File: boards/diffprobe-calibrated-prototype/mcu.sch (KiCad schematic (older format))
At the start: 2 parts

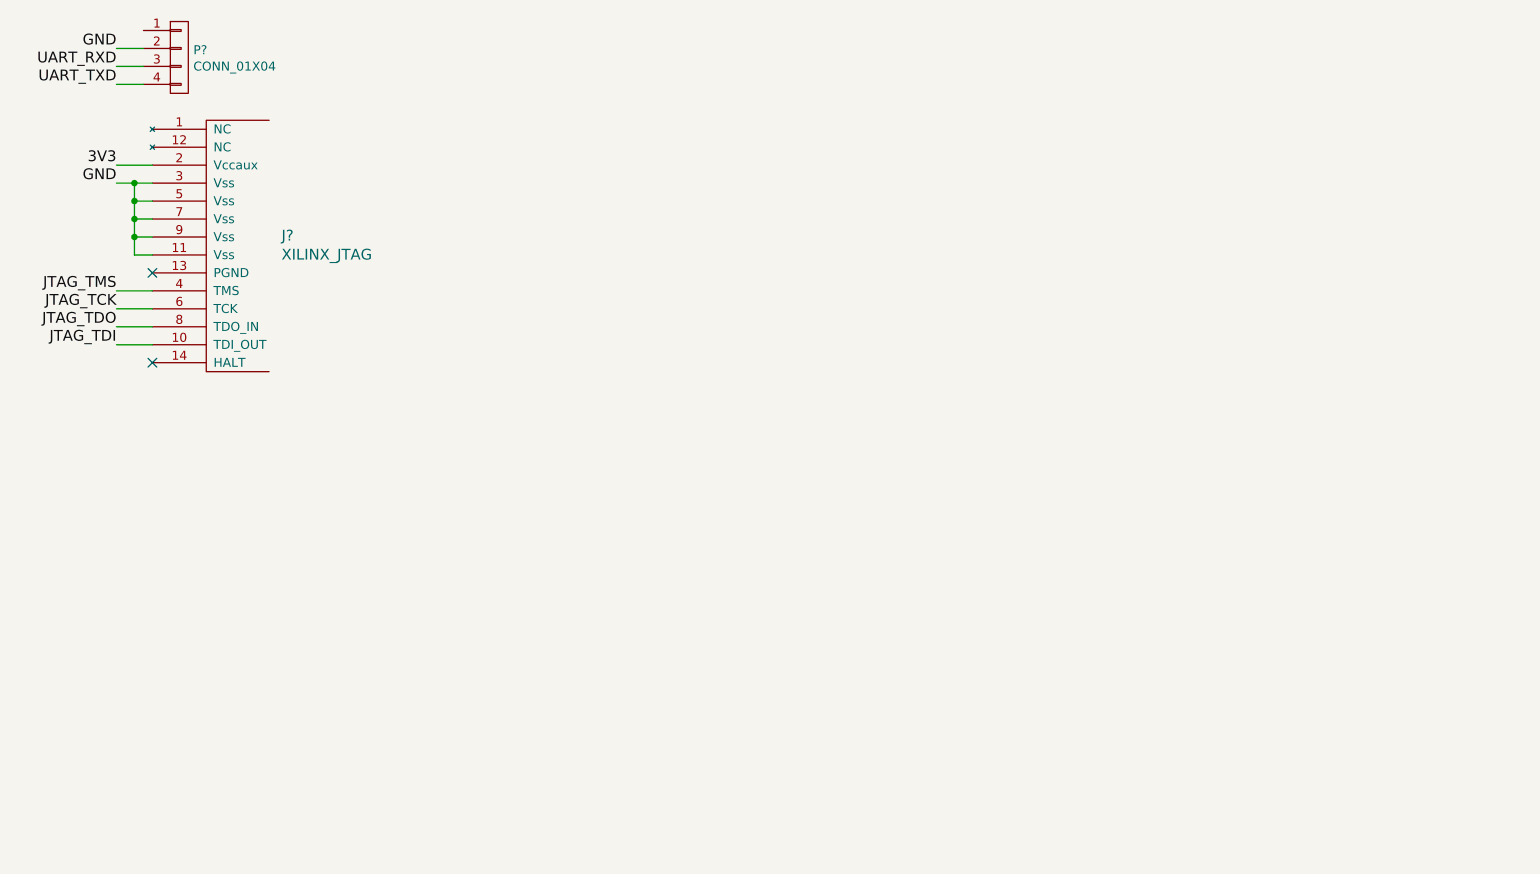
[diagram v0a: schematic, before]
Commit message: Continued work on differential probe
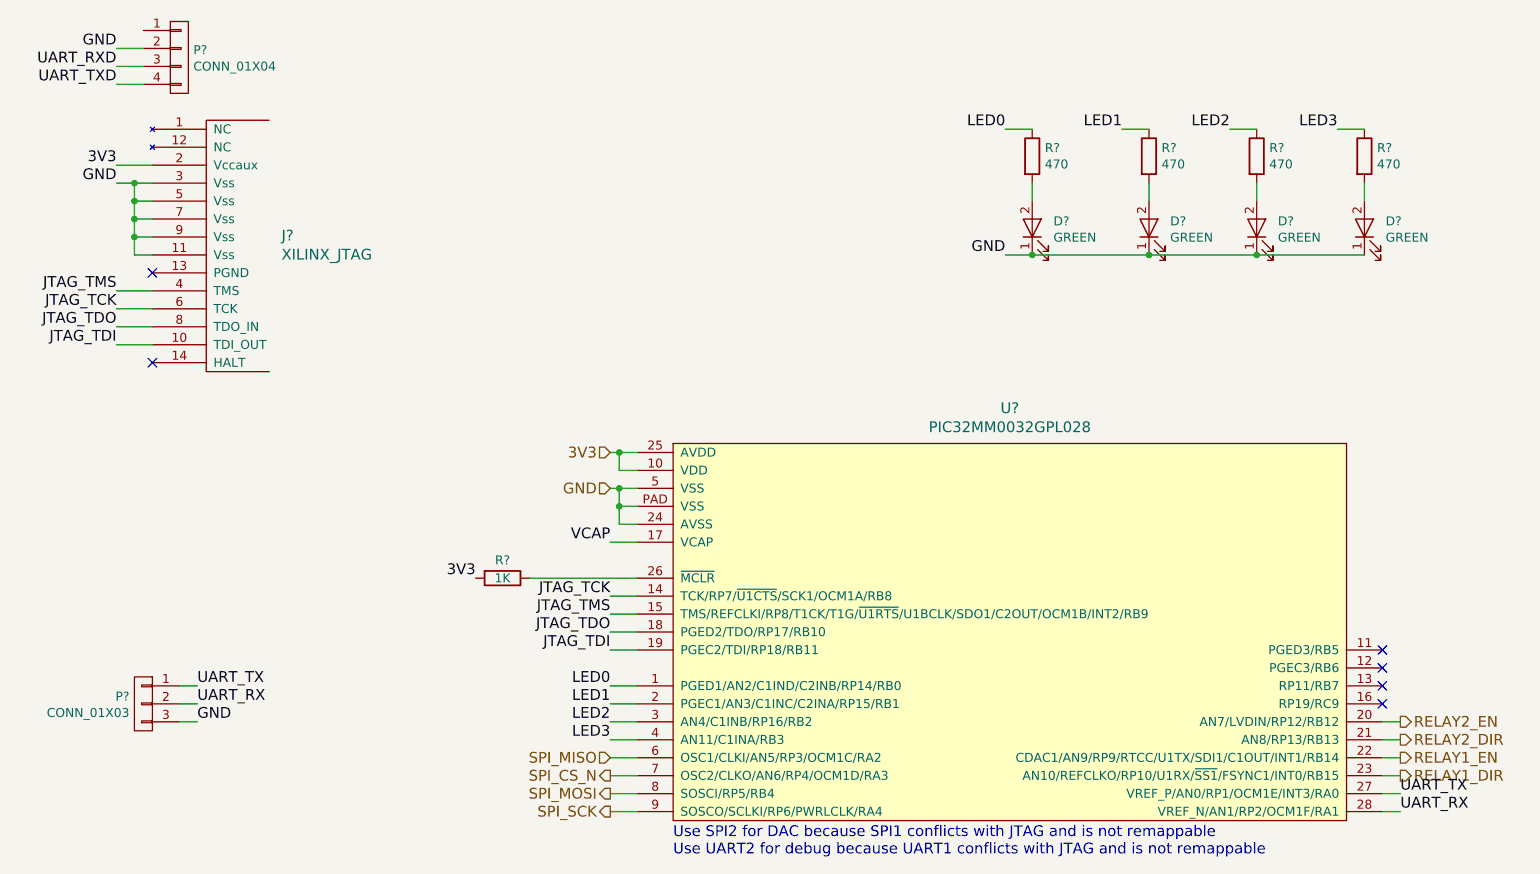
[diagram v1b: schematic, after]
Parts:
- added D? (x4): GREEN, symbol LED
- added P?: CONN_01X03, symbol CONN_01X03
- added R?: 1K, symbol R
- added R? (x4): 470, symbol R
- added U?: PIC32MM0032GPL028, symbol PIC32MMxGPL028
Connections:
- net 3V3: now also R?.2, U?.10 (VDD), U?.25 (AVDD)
- net GND: now also D?.1 (K), D?.1 (K), D?.1 (K), D?.1 (K), P?.3 (P3), U?.24 (AVSS), U?.5 (VSS), U?.PAD (VSS)
- net JTAG_TCK: now also U?.14 (TCK/RP7/~U1CTS~/SCK1/OCM1A/RB8)
- net JTAG_TDI: now also U?.19 (PGEC2/TDI/RP18/RB11)
- net JTAG_TDO: now also U?.18 (PGED2/TDO/RP17/RB10)
- net JTAG_TMS: now also U?.15 (TMS/REFCLKI/RP8/T1CK/T1G/~U1RTS~/U1BCLK/SDO1/C2OUT/OCM1B/INT2/RB9)
- new net: R?.1, U?.26 (~MCLR)
- new net: D?.2 (A), R?.2 (x4)
- new net LED0: R?.1, U?.1 (PGED1/AN2/C1IND/C2INB/RP14/RB0)
- new net LED1: R?.1, U?.2 (PGEC1/AN3/C1INC/C2INA/RP15/RB1)
- new net LED2: R?.1, U?.3 (AN4/C1INB/RP16/RB2)
- new net LED3: R?.1, U?.4 (AN11/C1INA/RB3)
- new net RELAY1_DIR: U?.23 (AN10/REFCLKO/RP10/U1RX/~SS1~/FSYNC1/INT0/RB15)
- new net RELAY1_EN: U?.22 (CDAC1/AN9/RP9/RTCC/U1TX/SDI1/C1OUT/INT1/RB14)
- new net RELAY2_DIR: U?.21 (AN8/RP13/RB13)
- new net RELAY2_EN: U?.20 (AN7/LVDIN/RP12/RB12)
- new net SPI_CS_N: U?.7 (OSC2/CLKO/AN6/RP4/OCM1D/RA3)
- new net SPI_MISO: U?.6 (OSC1/CLKI/AN5/RP3/OCM1C/RA2)
- new net SPI_MOSI: U?.8 (SOSCI/RP5/RB4)
- new net SPI_SCK: U?.9 (SOSCO/SCLKI/RP6/PWRLCLK/RA4)
- new net UART_RX: P?.2 (P2), U?.28 (VREF_N/AN1/RP2/OCM1F/RA1)
- new net UART_TX: P?.1 (P1), U?.27 (VREF_P/AN0/RP1/OCM1E/INT3/RA0)
- new net VCAP: U?.17 (VCAP)
- no-connect marks 2 -> 6
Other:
- note added: "Use SPI2 for DAC because SPI1 conflicts with JTAG and is not remappable\nUse UART2 for debug because UART1 conflicts with JTAG and is not remappable"

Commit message: Finished adding decoupling caps etc. Still needs signoff review.
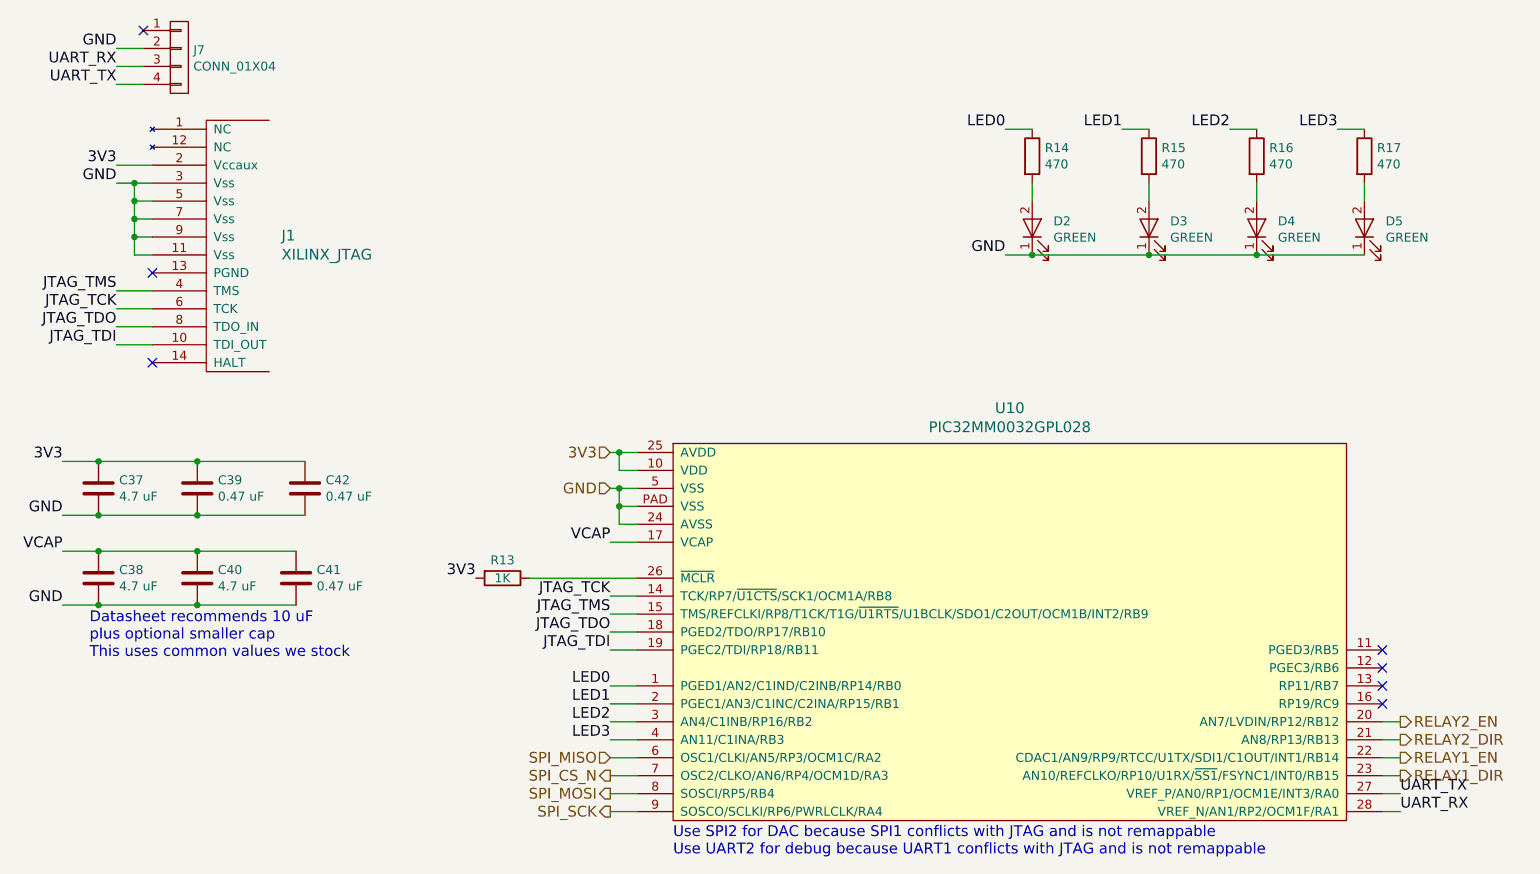
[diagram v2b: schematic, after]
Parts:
- removed P?: CONN_01X03, symbol CONN_01X03
- added C37, C38, C40: 4.7 uF, symbol C
- added C39, C41, C42: 0.47 uF, symbol C
- gave numbers to parts that had none: 12
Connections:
- net UART_RXD is gone; now on net UART_RX: J7.3 (P3)
- net UART_TXD is gone; now on net UART_TX: J7.4 (P4)
- net 3V3: now also C37.1, C39.1, C42.1
- net GND: now also C37.2, C38.2, C39.2, C40.2, C41.2, C42.2
- net VCAP: now also C38.1, C40.1, C41.1
- no-connect marks 6 -> 7
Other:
- note added: "Datasheet recommends 10 uF\nplus optional smaller cap\nThis uses common values we stock"
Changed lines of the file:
@@
 Sheet 4 4
 Title "500 MHz Active Differential Probe"
-Date "2017-12-18"
+Date "2017-12-19"
 Rev "0.2"
 Comp "Andrew D. Zonenberg"
@@
 $EndDescr
 $Comp
-L CONN_01X04 P?
+L CONN_01X04 J7
 U 1 1 5A1F8A2F
 P 1400 1100
-F 0 "P?" H 1478 1141 50  0000 L CNN
+F 0 "J7" H 1478 1141 50  0000 L CNN
 F 1 "CONN_01X04" H 1478 1050 50  0000 L CNN
 F 2 "" H 1400 1100 50  0000 C CNN
@@
 $EndComp
 Text Label 1050 1150 2    60   ~ 0
-UART_RXD
+UART_RX
 Wire Wire Line
 	1050 1050 1200 1050
@@
 	1050 1150 1200 1150
 Text Label 1050 1250 2    60   ~ 0
-UART_TXD
+UART_TX
 Wire Wire Line
 	1050 1250 1200 1250
 $Comp
-L XILINX_JTAG J?
+L XILINX_JTAG J1
 U 1 1 5A1F8B4D
 P 1250 2800
-F 0 "J?" H 1969 3508 60  0000 L CNN
+F 0 "J1" H 1969 3508 60  0000 L CNN
 F 1 "XILINX_JTAG" H 1969 3402 60  0000 L CNN
 F 2 "" H 1250 2800 60  0000 C CNN
@@
 NoConn ~ 1250 2800
 $Comp
-L PIC32MMxGPL028 U?
+L PIC32MMxGPL028 U10
 U 1 1 5A2E3505
 P 4150 5350
-F 0 "U?" H 6025 7647 60  0000 C CNN
+F 0 "U10" H 6025 7647 60  0000 C CNN
 F 1 "PIC32MM0032GPL028" H 6025 7541 60  0000 C CNN
 F 2 "" H 4150 5350 60  0001 C CNN
@@
 Wire Wire Line
 	3950 5300 3800 5300
-$Comp
-L CONN_01X03 P?
-U 1 1 5A363949
-P 1200 4700
-F 0 "P?" H 1278 4741 50  0000 L CNN
-F 1 "CONN_01X03" H 1278 4650 50  0000 L CNN
-F 2 "" H 1200 4700 50  0000 C CNN
-F 3 "" H 1200 4700 50  0000 C CNN
-	1    1200 4700
-	-1   0    0    -1
-$EndComp
-Text Label 1500 4600 0    60   ~ 0
-UART_TX
-Text Label 1500 4700 0    60   ~ 0
-UART_RX
-Text Label 1500 4800 0    60   ~ 0
-GND
 Text Label 1050 1050 2    60   ~ 0
 GND
-Wire Wire Line
-	1500 4600 1400 4600
-Wire Wire Line
-	1400 4700 1500 4700
-Wire Wire Line
-	1500 4800 1400 4800
 Text Label 8200 5200 0    60   ~ 0
 UART_TX
@@
 	8100 4900 8200 4900
 $Comp
-L R R?
+L R R13
 U 1 1 5A386F8B
 P 3200 4000
-F 0 "R?" V 3100 4000 50  0000 C CNN
+F 0 "R13" V 3100 4000 50  0000 C CNN
 F 1 "1K" V 3200 4000 50  0000 C CNN
 F 2 "" V 3130 4000 50  0000 C CNN
@@
 3V3
 $Comp
-L R R?
+L R R14
 U 1 1 5A3872CE
 P 6150 1650
-F 0 "R?" H 6220 1696 50  0000 L CNN
+F 0 "R14" H 6220 1696 50  0000 L CNN
 F 1 "470" H 6220 1605 50  0000 L CNN
 F 2 "" V 6080 1650 50  0000 C CNN
@@
 $EndComp
 $Comp
-L LED D?
+L LED D2
 U 1 1 5A387391
 P 6150 2050
-F 0 "D?" V 6188 1932 50  0000 R CNN
+F 0 "D2" V 6188 1932 50  0000 R CNN
 F 1 "GREEN" V 6097 1932 50  0000 R CNN
 F 2 "" H 6150 2050 50  0000 C CNN
@@
 	6000 2200 8000 2200
 $Comp
-L R R?
+L R R15
 U 1 1 5A3875D8
 P 6800 1650
-F 0 "R?" H 6870 1696 50  0000 L CNN
+F 0 "R15" H 6870 1696 50  0000 L CNN
 F 1 "470" H 6870 1605 50  0000 L CNN
 F 2 "" V 6730 1650 50  0000 C CNN
@@
 $EndComp
 $Comp
-L LED D?
+L LED D3
 U 1 1 5A3875DE
 P 6800 2050
-F 0 "D?" V 6838 1932 50  0000 R CNN
+F 0 "D3" V 6838 1932 50  0000 R CNN
 F 1 "GREEN" V 6747 1932 50  0000 R CNN
 F 2 "" H 6800 2050 50  0000 C CNN
@@
 	6650 1500 6800 1500
 $Comp
-L R R?
+L R R16
 U 1 1 5A387669
 P 7400 1650
-F 0 "R?" H 7470 1696 50  0000 L CNN
+F 0 "R16" H 7470 1696 50  0000 L CNN
 F 1 "470" H 7470 1605 50  0000 L CNN
 F 2 "" V 7330 1650 50  0000 C CNN
@@
 $EndComp
 $Comp
-L LED D?
+L LED D4
 U 1 1 5A38766F
 P 7400 2050
-F 0 "D?" V 7438 1932 50  0000 R CNN
+F 0 "D4" V 7438 1932 50  0000 R CNN
 F 1 "GREEN" V 7347 1932 50  0000 R CNN
 F 2 "" H 7400 2050 50  0000 C CNN
@@
 	7250 1500 7400 1500
 $Comp
-L R R?
+L R R17
 U 1 1 5A3876F8
 P 8000 1650
-F 0 "R?" H 8070 1696 50  0000 L CNN
+F 0 "R17" H 8070 1696 50  0000 L CNN
 F 1 "470" H 8070 1605 50  0000 L CNN
 F 2 "" V 7930 1650 50  0000 C CNN
@@
 $EndComp
 $Comp
-L LED D?
+L LED D5
 U 1 1 5A3876FE
 P 8000 2050
-F 0 "D?" V 8038 1932 50  0000 R CNN
+F 0 "D5" V 8038 1932 50  0000 R CNN
 F 1 "GREEN" V 7947 1932 50  0000 R CNN
 F 2 "" H 8000 2050 50  0000 C CNN
@@
 NoConn ~ 8100 4500
 NoConn ~ 8100 4400
+$Comp
+L C C37
+U 1 1 5A38C6FE
+P 950 3500
+F 0 "C37" H 1065 3546 50  0000 L CNN
+F 1 "4.7 uF" H 1065 3455 50  0000 L CNN
+F 2 "" H 988 3350 50  0000 C CNN
+F 3 "" H 950 3500 50  0000 C CNN
+	1    950  3500
+	1    0    0    -1
+$EndComp
+$Comp
+L C C39
+U 1 1 5A38C7B6
+P 1500 3500
+F 0 "C39" H 1615 3546 50  0000 L CNN
+F 1 "0.47 uF" H 1615 3455 50  0000 L CNN
+F 2 "" H 1538 3350 50  0000 C CNN
+F 3 "" H 1500 3500 50  0000 C CNN
+	1    1500 3500
+	1    0    0    -1
+$EndComp
+$Comp
+L C C42
+U 1 1 5A38C81E
+P 2100 3500
+F 0 "C42" H 2215 3546 50  0000 L CNN
+F 1 "0.47 uF" H 2215 3455 50  0000 L CNN
+F 2 "" H 2138 3350 50  0000 C CNN
+F 3 "" H 2100 3500 50  0000 C CNN
+	1    2100 3500
+	1    0    0    -1
+$EndComp
+Text Label 750  3350 2    60   ~ 0
+3V3
+Wire Wire Line
+	750  3350 2100 3350
+Connection ~ 950  3350
+Connection ~ 1500 3350
+Text Label 750  3650 2    60   ~ 0
+GND
+Wire Wire Line
+	750  3650 2100 3650
+Connection ~ 950  3650
+Connection ~ 1500 3650
+$Comp
+L C C38
+U 1 1 5A38CB75
+P 950 4000
+F 0 "C38" H 1065 4046 50  0000 L CNN
+F 1 "4.7 uF" H 1065 3955 50  0000 L CNN
+F 2 "" H 988 3850 50  0000 C CNN
+F 3 "" H 950 4000 50  0000 C CNN
+	1    950  4000
+	1    0    0    -1
+$EndComp
+$Comp
+L C C40
+U 1 1 5A38CBB9
+P 1500 4000
+F 0 "C40" H 1615 4046 50  0000 L CNN
+F 1 "4.7 uF" H 1615 3955 50  0000 L CNN
+F 2 "" H 1538 3850 50  0000 C CNN
+F 3 "" H 1500 4000 50  0000 C CNN
+	1    1500 4000
+	1    0    0    -1
+$EndComp
+Text Label 750  3850 2    60   ~ 0
+VCAP
+Text Label 750  4150 2    60   ~ 0
+GND
+Wire Wire Line
+	750  4150 2050 4150
+Connection ~ 950  4150
+Wire Wire Line
+	750  3850 2050 3850
+Connection ~ 950  3850
+$Comp
+L C C41
+U 1 1 5A38CDE8
+P 2050 4000
+F 0 "C41" H 2165 4046 50  0000 L CNN
+F 1 "0.47 uF" H 2165 3955 50  0000 L CNN
+F 2 "" H 2088 3850 50  0000 C CNN
+F 3 "" H 2050 4000 50  0000 C CNN
+	1    2050 4000
+	1    0    0    -1
+$EndComp
+Connection ~ 1500 3850
+Connection ~ 1500 4150
+Text Notes 900  4450 0    60   ~ 0
+Datasheet recommends 10 uF\nplus optional smaller cap\nThis uses common values we stock
+NoConn ~ 1200 950
 $EndSCHEMATC

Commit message: Initial layout
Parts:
- C37, C38, C40: footprint (none) -> azonenberg_pcb:EIA_0603_CAP_NOSILK
- C39, C41, C42: footprint (none) -> azonenberg_pcb:EIA_0402_CAP_NOSILK
- D2, D3, D4, D5: footprint (none) -> azonenberg_pcb:EIA_0402_LED
- J1: footprint (none) -> azonenberg_pcb:XILINX_JTAG_PTH_MOLEX_0878311420
- J7: footprint (none) -> azonenberg_pcb:CONN_HEADER_2.54MM_1x4
- R13, R14, R15, R16, R17: footprint (none) -> azonenberg_pcb:EIA_0402_RES_NOSILK
- U10: footprint (none) -> azonenberg_pcb:QFN_28_0.65MM_6x6MM
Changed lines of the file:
@@
 F 0 "J7" H 1478 1141 50  0000 L CNN
 F 1 "CONN_01X04" H 1478 1050 50  0000 L CNN
-F 2 "" H 1400 1100 50  0000 C CNN
+F 2 "azonenberg_pcb:CONN_HEADER_2.54MM_1x4" H 1400 1100 50  0001 C CNN
 F 3 "" H 1400 1100 50  0000 C CNN
 	1    1400 1100
@@
 F 0 "J1" H 1969 3508 60  0000 L CNN
 F 1 "XILINX_JTAG" H 1969 3402 60  0000 L CNN
-F 2 "" H 1250 2800 60  0000 C CNN
+F 2 "azonenberg_pcb:XILINX_JTAG_PTH_MOLEX_0878311420" H 1250 2800 60  0001 C CNN
 F 3 "" H 1250 2800 60  0000 C CNN
 	1    1250 2800
@@
 F 0 "U10" H 6025 7647 60  0000 C CNN
 F 1 "PIC32MM0032GPL028" H 6025 7541 60  0000 C CNN
-F 2 "" H 4150 5350 60  0001 C CNN
+F 2 "azonenberg_pcb:QFN_28_0.65MM_6x6MM" H 4150 5350 60  0001 C CNN
 F 3 "" H 4150 5350 60  0001 C CNN
 	1    4150 5350
@@
 F 0 "R13" V 3100 4000 50  0000 C CNN
 F 1 "1K" V 3200 4000 50  0000 C CNN
-F 2 "" V 3130 4000 50  0000 C CNN
+F 2 "azonenberg_pcb:EIA_0402_RES_NOSILK" V 3130 4000 50  0001 C CNN
 F 3 "" H 3200 4000 50  0000 C CNN
 	1    3200 4000
@@
 F 0 "R14" H 6220 1696 50  0000 L CNN
 F 1 "470" H 6220 1605 50  0000 L CNN
-F 2 "" V 6080 1650 50  0000 C CNN
+F 2 "azonenberg_pcb:EIA_0402_RES_NOSILK" V 6080 1650 50  0001 C CNN
 F 3 "" H 6150 1650 50  0000 C CNN
 	1    6150 1650
@@
 F 0 "D2" V 6188 1932 50  0000 R CNN
 F 1 "GREEN" V 6097 1932 50  0000 R CNN
-F 2 "" H 6150 2050 50  0000 C CNN
+F 2 "azonenberg_pcb:EIA_0402_LED" H 6150 2050 50  0001 C CNN
 F 3 "" H 6150 2050 50  0000 C CNN
 	1    6150 2050
@@
 F 0 "R15" H 6870 1696 50  0000 L CNN
 F 1 "470" H 6870 1605 50  0000 L CNN
-F 2 "" V 6730 1650 50  0000 C CNN
+F 2 "azonenberg_pcb:EIA_0402_RES_NOSILK" V 6730 1650 50  0001 C CNN
 F 3 "" H 6800 1650 50  0000 C CNN
 	1    6800 1650
@@
 F 0 "D3" V 6838 1932 50  0000 R CNN
 F 1 "GREEN" V 6747 1932 50  0000 R CNN
-F 2 "" H 6800 2050 50  0000 C CNN
+F 2 "azonenberg_pcb:EIA_0402_LED" H 6800 2050 50  0001 C CNN
 F 3 "" H 6800 2050 50  0000 C CNN
 	1    6800 2050
@@
 F 0 "R16" H 7470 1696 50  0000 L CNN
 F 1 "470" H 7470 1605 50  0000 L CNN
-F 2 "" V 7330 1650 50  0000 C CNN
+F 2 "azonenberg_pcb:EIA_0402_RES_NOSILK" V 7330 1650 50  0001 C CNN
 F 3 "" H 7400 1650 50  0000 C CNN
 	1    7400 1650
@@
 F 0 "D4" V 7438 1932 50  0000 R CNN
 F 1 "GREEN" V 7347 1932 50  0000 R CNN
-F 2 "" H 7400 2050 50  0000 C CNN
+F 2 "azonenberg_pcb:EIA_0402_LED" H 7400 2050 50  0001 C CNN
 F 3 "" H 7400 2050 50  0000 C CNN
 	1    7400 2050
@@
 F 0 "R17" H 8070 1696 50  0000 L CNN
 F 1 "470" H 8070 1605 50  0000 L CNN
-F 2 "" V 7930 1650 50  0000 C CNN
+F 2 "azonenberg_pcb:EIA_0402_RES_NOSILK" V 7930 1650 50  0001 C CNN
 F 3 "" H 8000 1650 50  0000 C CNN
 	1    8000 1650
@@
 F 0 "D5" V 8038 1932 50  0000 R CNN
 F 1 "GREEN" V 7947 1932 50  0000 R CNN
-F 2 "" H 8000 2050 50  0000 C CNN
+F 2 "azonenberg_pcb:EIA_0402_LED" H 8000 2050 50  0001 C CNN
 F 3 "" H 8000 2050 50  0000 C CNN
 	1    8000 2050
@@
 F 0 "C37" H 1065 3546 50  0000 L CNN
 F 1 "4.7 uF" H 1065 3455 50  0000 L CNN
-F 2 "" H 988 3350 50  0000 C CNN
+F 2 "azonenberg_pcb:EIA_0603_CAP_NOSILK" H 988 3350 50  0001 C CNN
 F 3 "" H 950 3500 50  0000 C CNN
 	1    950  3500
@@
 F 0 "C39" H 1615 3546 50  0000 L CNN
 F 1 "0.47 uF" H 1615 3455 50  0000 L CNN
-F 2 "" H 1538 3350 50  0000 C CNN
+F 2 "azonenberg_pcb:EIA_0402_CAP_NOSILK" H 1538 3350 50  0001 C CNN
 F 3 "" H 1500 3500 50  0000 C CNN
 	1    1500 3500
@@
 F 0 "C42" H 2215 3546 50  0000 L CNN
 F 1 "0.47 uF" H 2215 3455 50  0000 L CNN
-F 2 "" H 2138 3350 50  0000 C CNN
+F 2 "azonenberg_pcb:EIA_0402_CAP_NOSILK" H 2138 3350 50  0001 C CNN
 F 3 "" H 2100 3500 50  0000 C CNN
 	1    2100 3500
@@
 F 0 "C38" H 1065 4046 50  0000 L CNN
 F 1 "4.7 uF" H 1065 3955 50  0000 L CNN
-F 2 "" H 988 3850 50  0000 C CNN
+F 2 "azonenberg_pcb:EIA_0603_CAP_NOSILK" H 988 3850 50  0001 C CNN
 F 3 "" H 950 4000 50  0000 C CNN
 	1    950  4000
@@
 F 0 "C40" H 1615 4046 50  0000 L CNN
 F 1 "4.7 uF" H 1615 3955 50  0000 L CNN
-F 2 "" H 1538 3850 50  0000 C CNN
+F 2 "azonenberg_pcb:EIA_0603_CAP_NOSILK" H 1538 3850 50  0001 C CNN
 F 3 "" H 1500 4000 50  0000 C CNN
 	1    1500 4000
@@
 F 0 "C41" H 2165 4046 50  0000 L CNN
 F 1 "0.47 uF" H 2165 3955 50  0000 L CNN
-F 2 "" H 2088 3850 50  0000 C CNN
+F 2 "azonenberg_pcb:EIA_0402_CAP_NOSILK" H 2088 3850 50  0001 C CNN
 F 3 "" H 2050 4000 50  0000 C CNN
 	1    2050 4000
